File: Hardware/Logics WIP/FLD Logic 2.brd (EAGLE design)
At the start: 61 x 33 mm, 82 parts

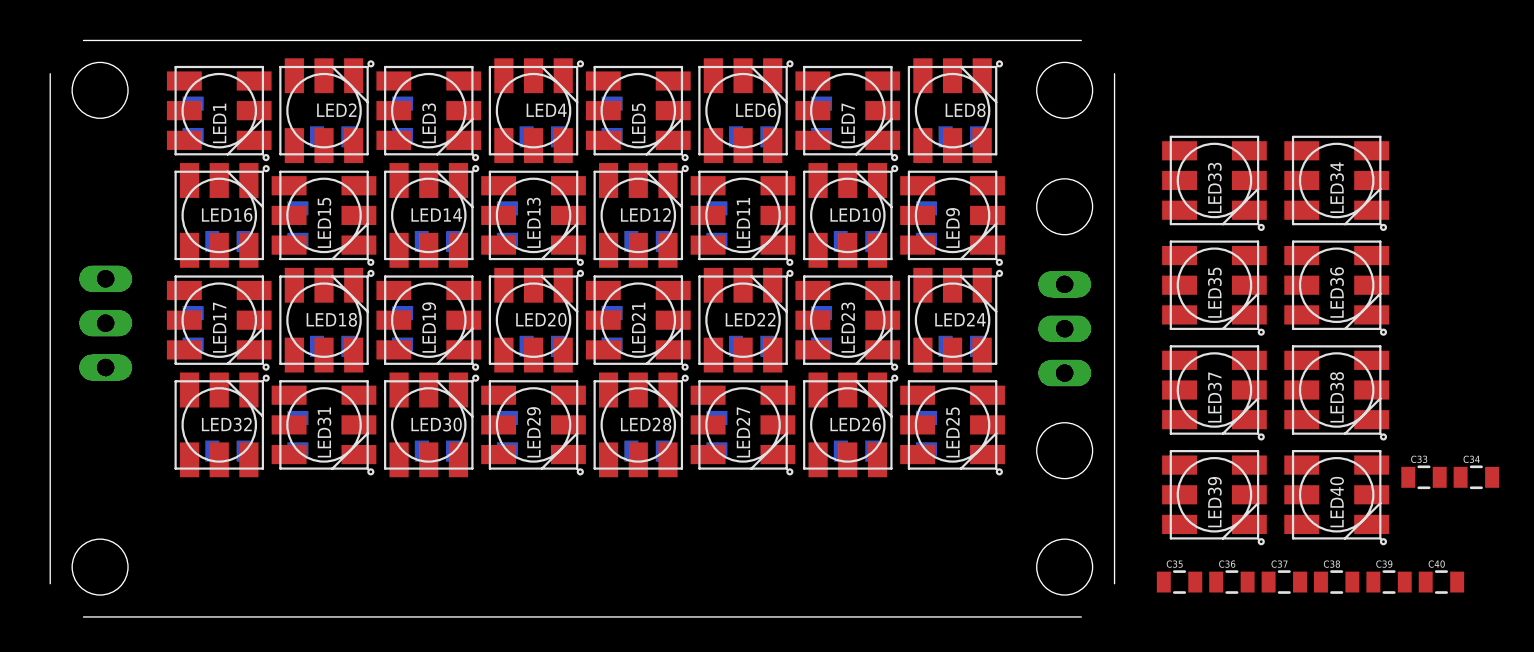
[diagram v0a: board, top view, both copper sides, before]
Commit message: 
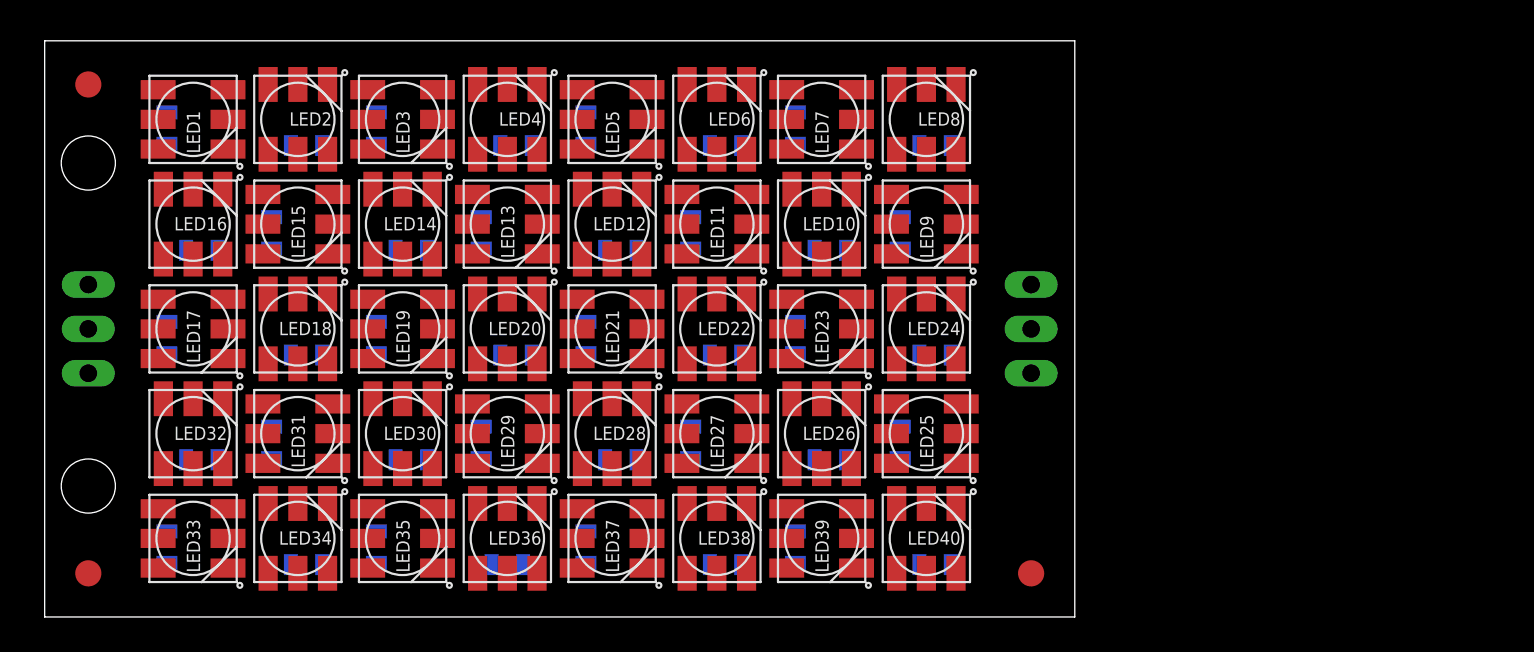
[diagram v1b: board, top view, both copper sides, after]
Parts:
- added FID1, FID2, FID3: FIDUCIAL1.5X3, SparkFun-Aesthetics:FIDUCIAL-1.5X3
- C1, C10, C11, C12, C13, C14, C15, C16, C17, C18, C19, C2, C20, C21, C22, C23, C24, C25, C26, C27, C28, C29, C3, C30, C31, C32, C33, C34, C35, C36, C37, C38, C39, C4, C40, C5, C6, C7, C8, C9: value (none) -> 0.1uF
- moved C33 72.1 mm to (7.00, 4.00), flipped to the bottom, turned to 270 degrees
- moved C34 67.2 mm to (15.0, 3.00), flipped to the bottom, turned to 180 degrees
- moved LED34 62.9 mm to (14.5, 4.50), turned to 90 degrees
- moved LED33 62.0 mm to (8.50, 4.50)
- moved IN 55.9 mm to (2.50, 16.5)
- moved OUT 53.0 mm to (56.5, 16.5)
- moved LED36 49.7 mm to (26.5, 4.50), turned to 90 degrees
- moved LED35 48.7 mm to (20.5, 4.50)
- moved C35 46.0 mm to (19.0, 4.00), flipped to the bottom, turned to 270 degrees
- moved C36 41.5 mm to (26.5, 3.00), flipped to the bottom, turned to 180 degrees
- moved C37 40.0 mm to (31.0, 4.00), flipped to the bottom, turned to 270 degrees
- moved LED38 36.5 mm to (38.5, 4.50), turned to 90 degrees
- moved LED37 35.5 mm to (32.5, 4.50)
- moved C38 35.0 mm to (39.0, 3.00), flipped to the bottom, turned to 180 degrees
- moved C39 34.1 mm to (43.0, 4.00), flipped to the bottom, turned to 270 degrees
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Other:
- board size 61 x 33 mm -> 59 x 33 mm

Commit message: 
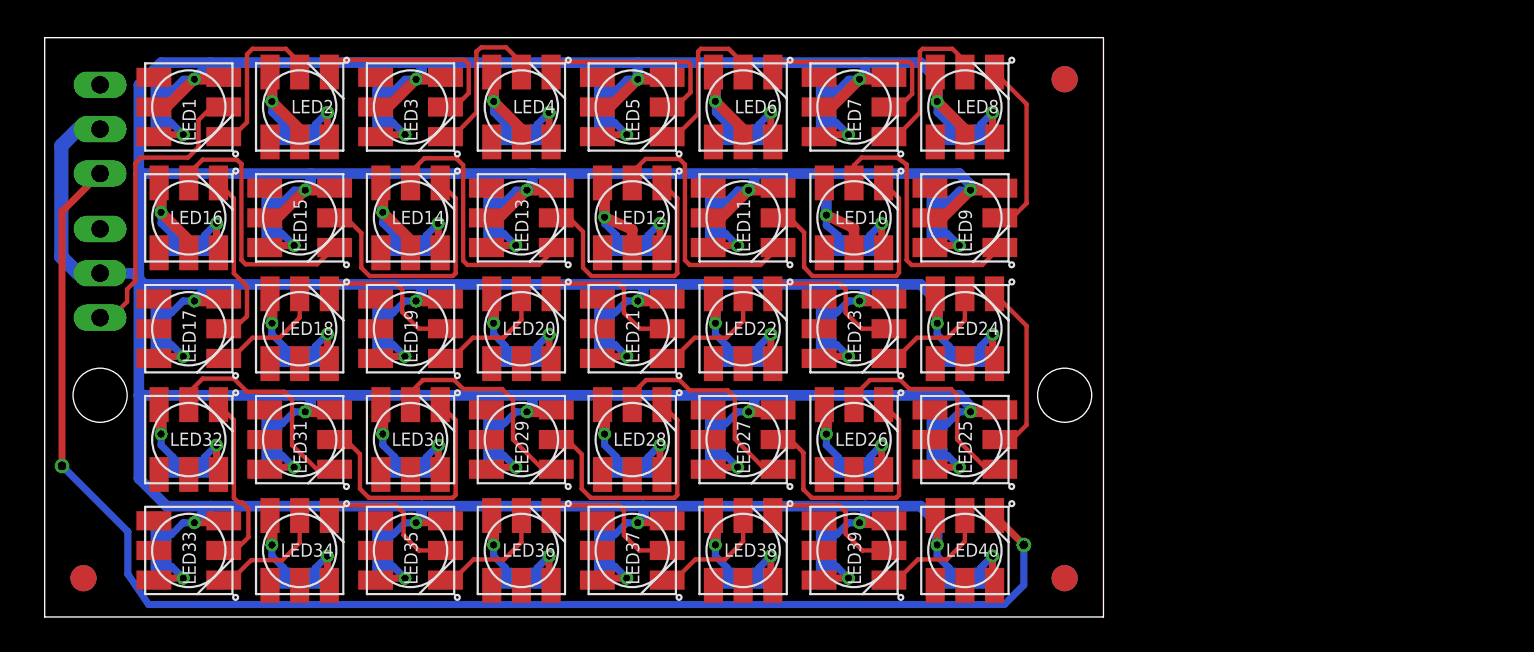
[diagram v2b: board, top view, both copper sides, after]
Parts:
- added FID4, FID5, FID6: FIDUCIAL1.5X3, SparkFun-Aesthetics:FIDUCIAL-1.5X3
- moved FID1 55.9 mm to (58.4, 30.8)
- moved FID3 55.9 mm to (58.4, 2.22)
- moved OUT 54.5 mm to (3.17, 27.9)
- moved FID2 54.3 mm to (2.22, 2.22)
- moved IN 3.26 mm to (3.17, 19.7)
- moved LED8 2.32 mm to (52.7, 29.2)
- moved LED40 2.31 mm to (52.7, 3.81)
- moved C9 2.29 mm to (51.1, 22.9)
- moved LED9 2.23 mm to (52.7, 22.9)
- moved LED25 2.23 mm to (52.7, 10.2)
- moved LED24 2.21 mm to (52.7, 16.5)
- moved C7 2.14 mm to (44.8, 29.2)
- moved C25 2.12 mm to (51.1, 10.2)
- moved LED7 1.99 mm to (46.4, 29.2)
- moved LED39 1.98 mm to (46.4, 3.81)
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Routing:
- net +5V: track 0.00 -> 538.0 mm, vias 0 -> 40
- net GND: track 0.00 -> 131.4 mm, vias 0 -> 40
- net DOUT: track 0.00 -> 82.8 mm, vias 0 -> 2
- net DIN: track 0.00 -> 17.4 mm
- net N$8: track 0.00 -> 15.7 mm
- net N$11: track 0.00 -> 15.5 mm
- net N$9: track 0.00 -> 15.4 mm
- net N$12: track 0.00 -> 15.3 mm
- net N$24: track 0.00 -> 15.1 mm
- net N$14: track 0.00 -> 15.1 mm
- net N$10: track 0.00 -> 15.1 mm
- net N$28: track 0.00 -> 15.1 mm
- net N$13: track 0.00 -> 15.1 mm
- net N$27: track 0.00 -> 15.1 mm
- net N$26: track 0.00 -> 13.0 mm
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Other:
- board size 59 x 33 mm -> 60.6 x 33.2 mm

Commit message: 
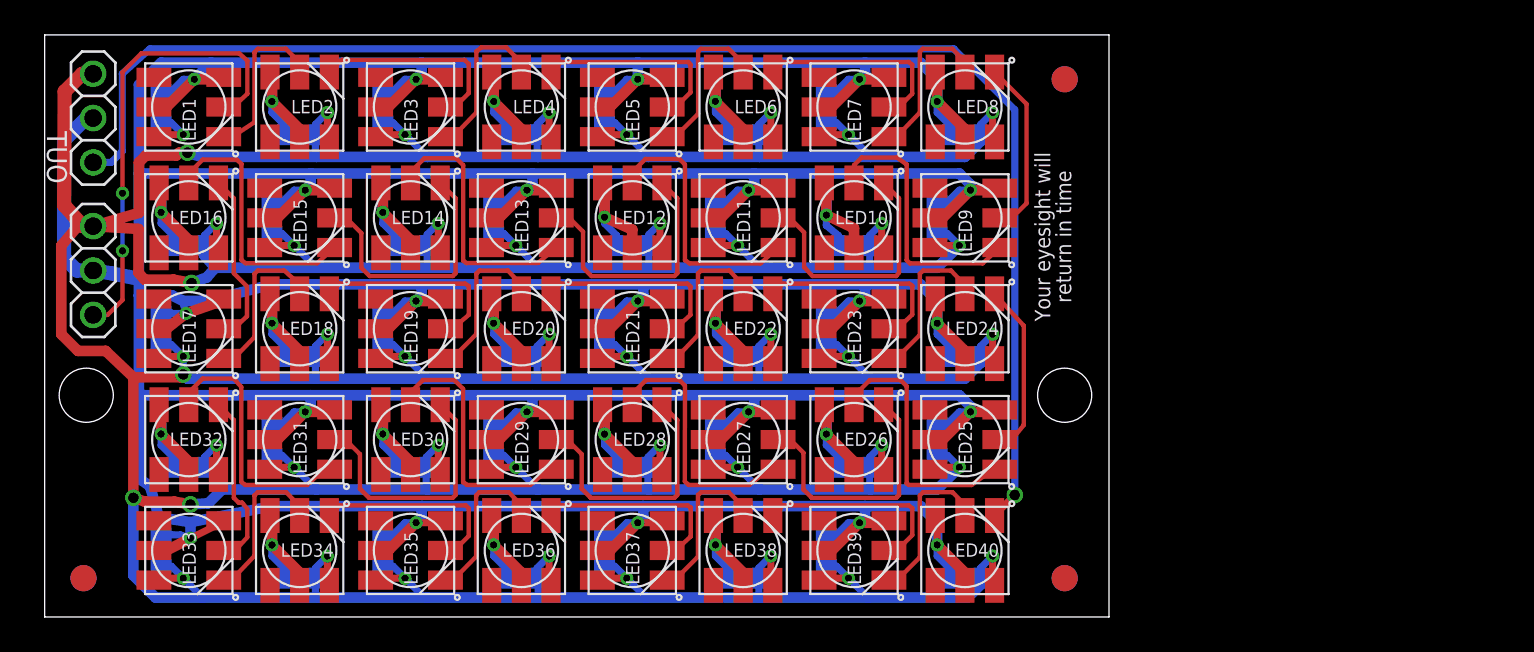
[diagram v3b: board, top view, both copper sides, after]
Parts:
- IN, OUT: device pinhead:1X03 -> adafruit:1X03
- moved OUT 0.75 mm to (2.78, 28.6), flipped to the top
- moved IN 0.43 mm to (2.78, 19.8), flipped to the top
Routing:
- net GND: track 131.4 -> 473.6 mm, vias 40 -> 45
- net +5V: track 538.0 -> 608.7 mm
- net DIN: track 17.4 -> 26.4 mm, vias 0 -> 2
- net N$17: track 8.70 -> 11.6 mm
- net N$34: track 8.70 -> 11.6 mm
- net N$20: track 8.75 -> 11.6 mm
- net N$37: track 8.70 -> 11.5 mm
- net N$38: track 8.80 -> 11.6 mm
- net N$21: track 8.77 -> 11.6 mm
- net N$15: track 6.68 -> 9.41 mm
- net N$36: track 6.75 -> 9.43 mm
- net N$33: track 6.78 -> 9.40 mm
- net N$35: track 6.75 -> 9.36 mm
- net N$16: track 6.75 -> 9.33 mm
- net N$18: track 6.80 -> 9.37 mm
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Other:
- board size 60.6 x 33.2 mm -> 61 x 33.3 mm
- board text added: "Your eyesight will return in time"

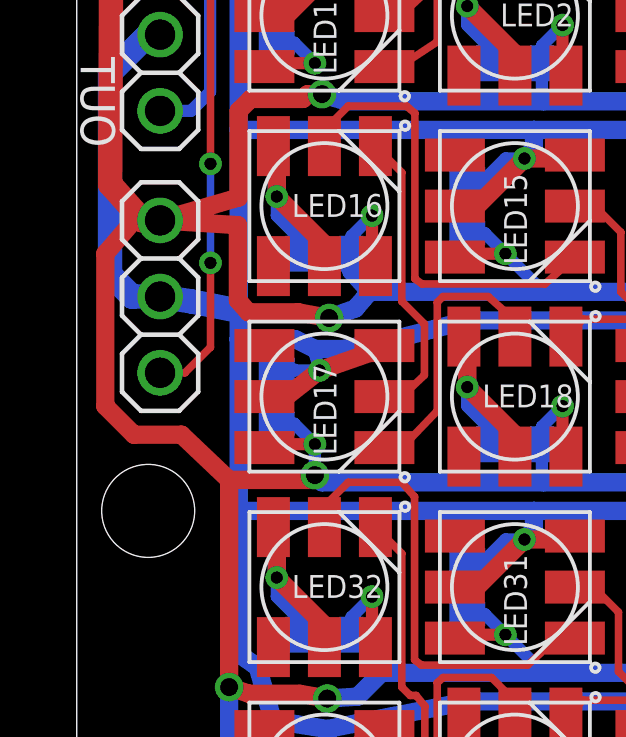
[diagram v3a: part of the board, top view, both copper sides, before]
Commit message: 
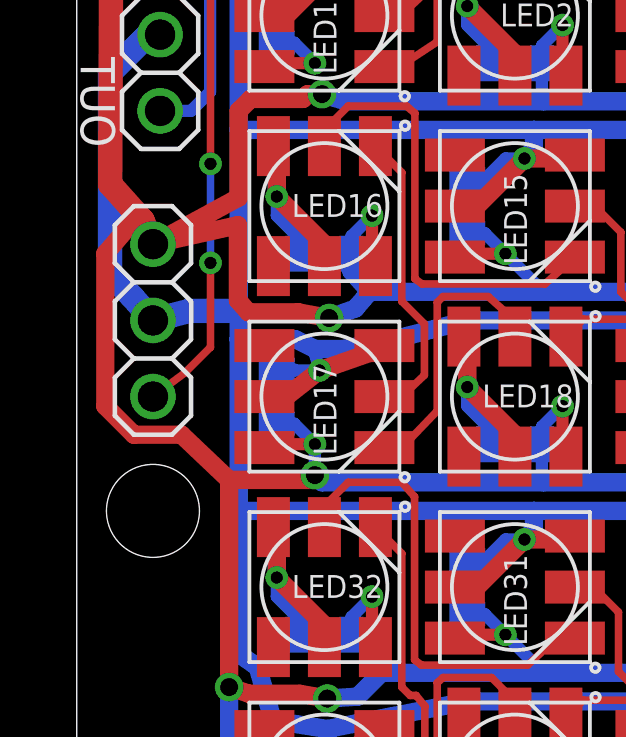
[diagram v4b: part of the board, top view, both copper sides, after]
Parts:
- moved IN 0.83 mm to (2.54, 19.1)
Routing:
- net GND: track 473.6 -> 474.7 mm
- net DIN: track 26.4 -> 26.9 mm
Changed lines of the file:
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@@
 <wire x1="60.96" y1="33.3375" x2="60.96" y2="0" width="0" layer="20"/>
 <wire x1="60.96" y1="0" x2="0" y2="0" width="0" layer="20"/>
-<hole x="2.38125" y="12.7" drill="3.1"/>
+<hole x="2.54" y="12.7" drill="3.1"/>
 <hole x="58.42" y="12.7" drill="3.1"/>
 <text x="57.75325" y="21.7805" size="0.889" layer="21" font="vector" distance="35" rot="R90" align="center">Your eyesight will
@@
 <element name="FID5" library="SparkFun-Aesthetics" package="FIDUCIAL-1.5X3" value="FIDUCIAL1.5X3" x="58.42" y="2.2225" rot="MR0"/>
 <element name="FID6" library="SparkFun-Aesthetics" package="FIDUCIAL-1.5X3" value="FIDUCIAL1.5X3" x="2.2225" y="2.2225" rot="MR0"/>
-<element name="IN" library="adafruit" package="1X03" value="" x="2.778125" y="19.84375" smashed="yes" rot="R270">
-<attribute name="NAME" x="1.209675" y="18.20545" size="1.143" layer="26" font="vector" ratio="10" rot="MR270"/>
-<attribute name="VALUE" x="-0.396875" y="23.65375" size="1.27" layer="27" rot="R270"/>
+<element name="IN" library="adafruit" package="1X03" value="" x="2.54" y="19.05" smashed="yes" rot="R270">
+<attribute name="NAME" x="0.97155" y="17.4117" size="1.143" layer="26" font="vector" ratio="10" rot="MR270"/>
+<attribute name="VALUE" x="-0.635" y="22.86" size="1.27" layer="27" rot="R270"/>
 </element>
 <element name="OUT" library="adafruit" package="1X03" value="" x="2.778125" y="28.575" smashed="yes" rot="R270">
@@
 <wire x1="1.143" y1="30.099" x2="1.11125" y2="23.59025" width="0.8128" layer="1"/>
 <wire x1="1.11125" y1="23.59025" x2="2.19075" y2="22.38375" width="0.8128" layer="1"/>
-<wire x1="2.19075" y1="22.38375" x2="2.778125" y2="22.38375" width="0.8128" layer="1"/>
+<wire x1="2.19075" y1="22.38375" x2="2.54" y2="21.59" width="0.8128" layer="1"/>
 <wire x1="5.08" y1="13.731875" x2="7.77875" y2="13.731875" width="0.6096" layer="1"/>
 <wire x1="7.77875" y1="13.731875" x2="7.9375" y2="13.890625" width="0.6096" layer="1"/>
@@
 <wire x1="5.794375" y1="26.431875" x2="5.3975" y2="26.035" width="0.6096" layer="1"/>
 <wire x1="5.3975" y1="26.035" x2="5.3975" y2="23.14575" width="0.6096" layer="1"/>
-<wire x1="5.3975" y1="23.14575" x2="2.778125" y2="22.38375" width="0.6096" layer="1"/>
+<wire x1="5.3975" y1="23.14575" x2="2.54" y2="21.59" width="0.6096" layer="1"/>
 <wire x1="9.763125" y1="20.0025" x2="9.286875" y2="19.446875" width="0.6096" layer="16"/>
 <wire x1="9.286875" y1="19.446875" x2="8.41375" y2="19.129375" width="0.6096" layer="16"/>
@@
 <wire x1="5.72135" y1="19.319875" x2="5.3721" y2="19.7231" width="0.6096" layer="1"/>
 <wire x1="5.3721" y1="19.7231" x2="5.3721" y2="22.225" width="0.6096" layer="1"/>
-<wire x1="5.3721" y1="22.225" x2="2.778125" y2="22.38375" width="0.6096" layer="1"/>
+<wire x1="5.3721" y1="22.225" x2="2.54" y2="21.59" width="0.6096" layer="1"/>
 <wire x1="9.763125" y1="20.0025" x2="9.155" y2="20.69" width="0.6096" layer="16"/>
 <wire x1="9.155" y1="20.69" x2="9.155" y2="21.2725" width="0.6096" layer="16"/>
@@
 <wire x1="1.11125" y1="27.305" x2="1.11125" y2="20.574" width="0.8128" layer="16"/>
 <wire x1="1.11125" y1="20.574" x2="1.8415" y2="19.84375" width="0.8128" layer="16"/>
-<wire x1="1.8415" y1="19.84375" x2="2.778125" y2="19.84375" width="0.8128" layer="16"/>
+<wire x1="1.8415" y1="19.84375" x2="2.54" y2="19.05" width="0.8128" layer="16"/>
 <wire x1="44.655" y1="24.86" x2="44.7675" y2="24.7475" width="0.6096" layer="1"/>
 <wire x1="44.7675" y1="24.7475" x2="44.7675" y2="23.01875" width="0.6096" layer="1"/>
 <wire x1="52.705" y1="14.51" x2="52.705" y2="15.24" width="0.6096" layer="1"/>
 <wire x1="52.705" y1="15.24" x2="51.1175" y2="16.8275" width="0.6096" layer="1"/>
-<wire x1="5.3975" y1="19.3675" x2="3.81" y2="19.685" width="0.8128" layer="16"/>
-<wire x1="3.81" y1="19.685" x2="2.778125" y2="19.84375" width="0.8128" layer="16"/>
+<wire x1="5.3975" y1="19.3675" x2="3.7465" y2="19.3675" width="0.8128" layer="16"/>
+<wire x1="3.7465" y1="19.3675" x2="2.54" y2="19.05" width="0.8128" layer="16"/>
 <wire x1="5.3975" y1="18.415" x2="5.3975" y2="19.3675" width="0.6096" layer="16"/>
 <wire x1="10.556875" y1="18.415" x2="8.89" y2="18.0975" width="0.6096" layer="16"/>
@@
 <wire x1="4.4577" y1="20.9677" x2="4.4577" y2="18.15465" width="0.254" layer="1"/>
 <wire x1="4.4577" y1="18.15465" x2="3.6068" y2="17.30375" width="0.254" layer="1"/>
-<wire x1="3.6068" y1="17.30375" x2="2.778125" y2="17.30375" width="0.254" layer="1"/>
+<wire x1="3.6068" y1="17.30375" x2="2.54" y2="16.51" width="0.254" layer="1"/>
 </signal>
 <signal name="N$1">
